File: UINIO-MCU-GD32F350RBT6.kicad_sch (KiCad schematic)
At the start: 31 parts, among them J1 Conn_01x32_Pin, J2 Conn_01x32_Pin, J3 Conn_01x04_Pin, SW1 BOOT0, SW2 NRST, U1 ME6211C33M5G-N, U2 GD32F350RBT6, Y1 32.768KHz, Y2 8MHz

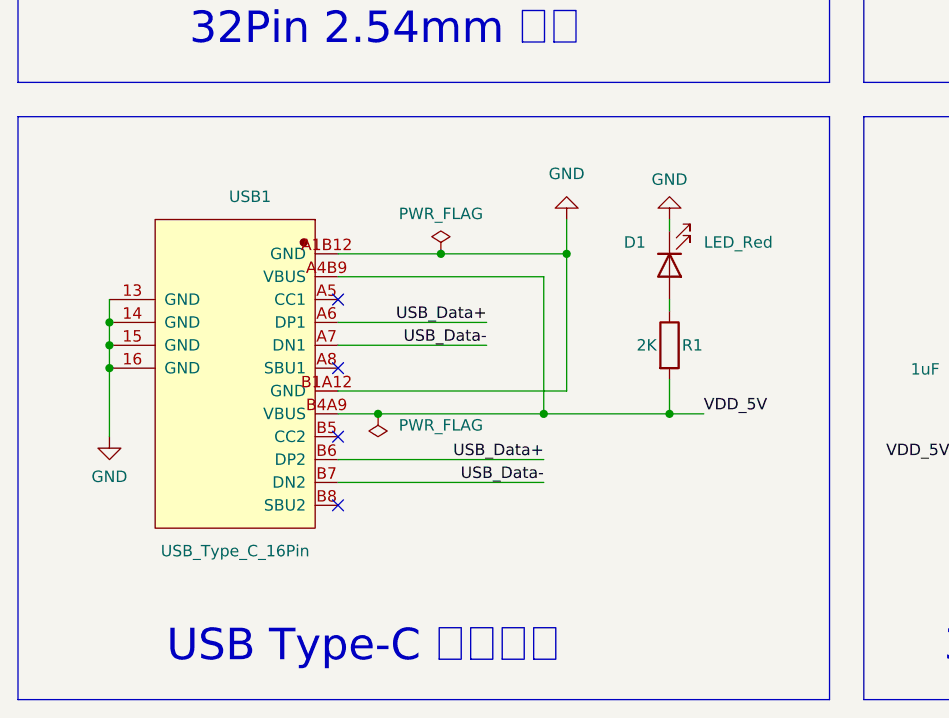
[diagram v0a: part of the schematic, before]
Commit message: Release UINIO-MCU-GD32F350RBT6 version 3.0.0.
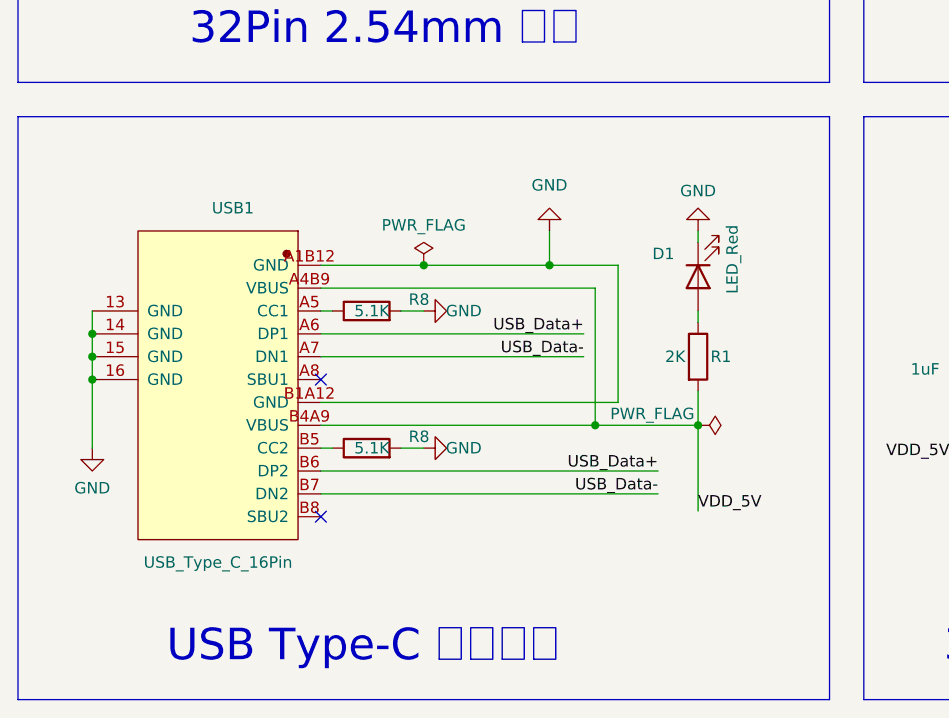
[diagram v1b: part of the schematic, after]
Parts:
- added R8 (x2): 5.1K, Resistor_SMD:R_0603_1608Metric, symbol Device:R
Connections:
- net GND: now also R8.2, R8.2
- net at USB1.A5 (CC1): now also R8.1
- net at USB1.B5 (CC2): now also R8.1
- no-connect marks 5 -> 3
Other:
- moved on the sheet: D1, R1, USB1

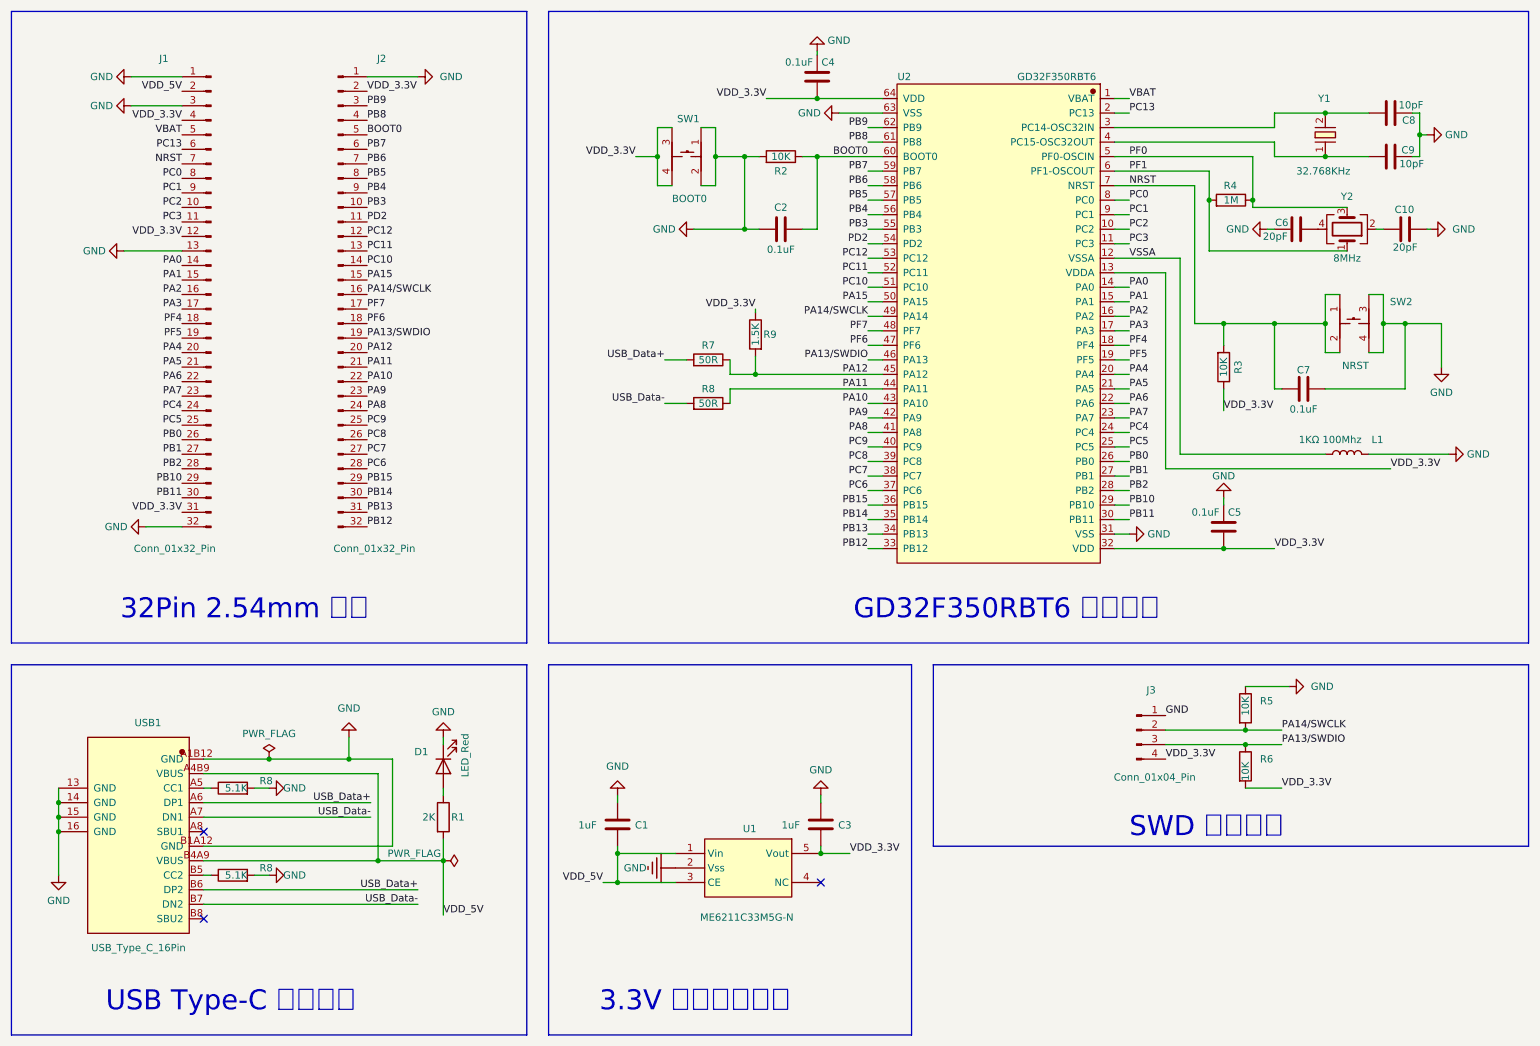
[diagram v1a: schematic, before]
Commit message: Release UINIO-MCU-GD32F350RBT6 version 3.0.1.
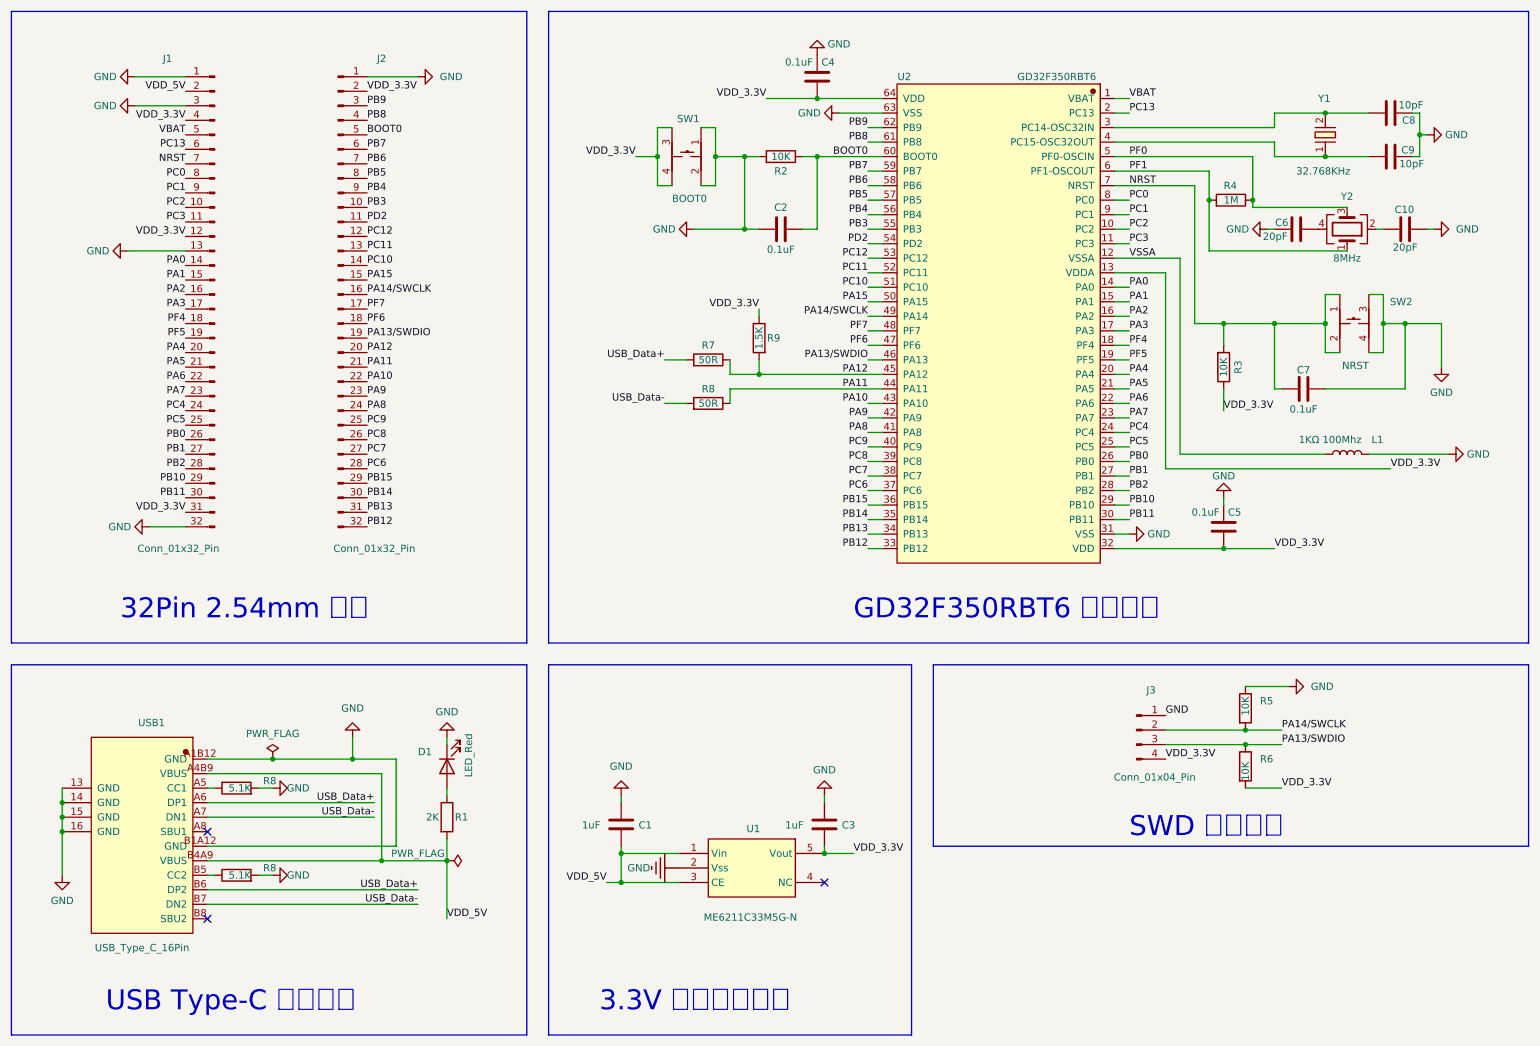
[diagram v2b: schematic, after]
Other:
- company: 电子技术博客 UinIO.com -> UinIO.com 电子技术实验室
- moved on the sheet: C1, C3, D1, J1, R1, R8, R9, U1, USB1

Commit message: Release UINIO-MCU-GD32F350RBT6 version 3.1.1.
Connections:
- net VDD_3.3V: now also R1.2
- net VDD_5V: no longer R1.2
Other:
- moved on the sheet: C1, C3, D1, R1, U1
